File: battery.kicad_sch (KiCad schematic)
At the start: 27 parts, among them J2 Conn_01x02, U7 MP2637GR-P, U8 MAX17048G+T10

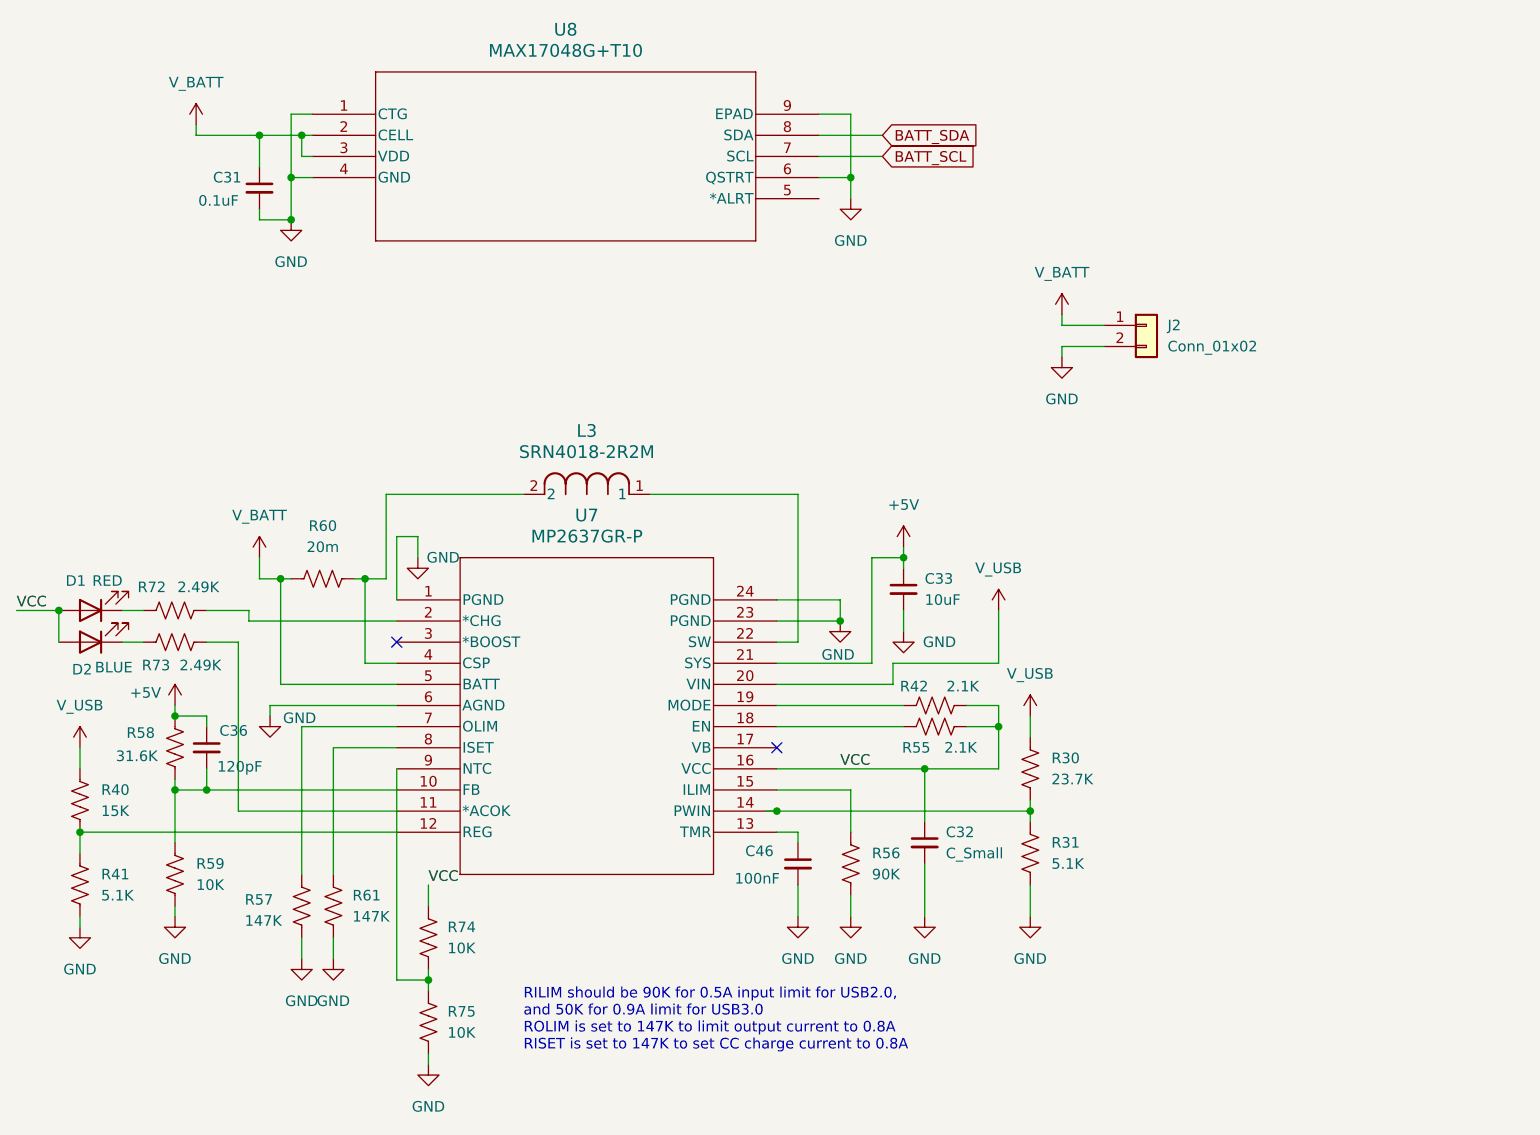
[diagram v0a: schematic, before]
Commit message: All footprints configured correctly. Next step is layout
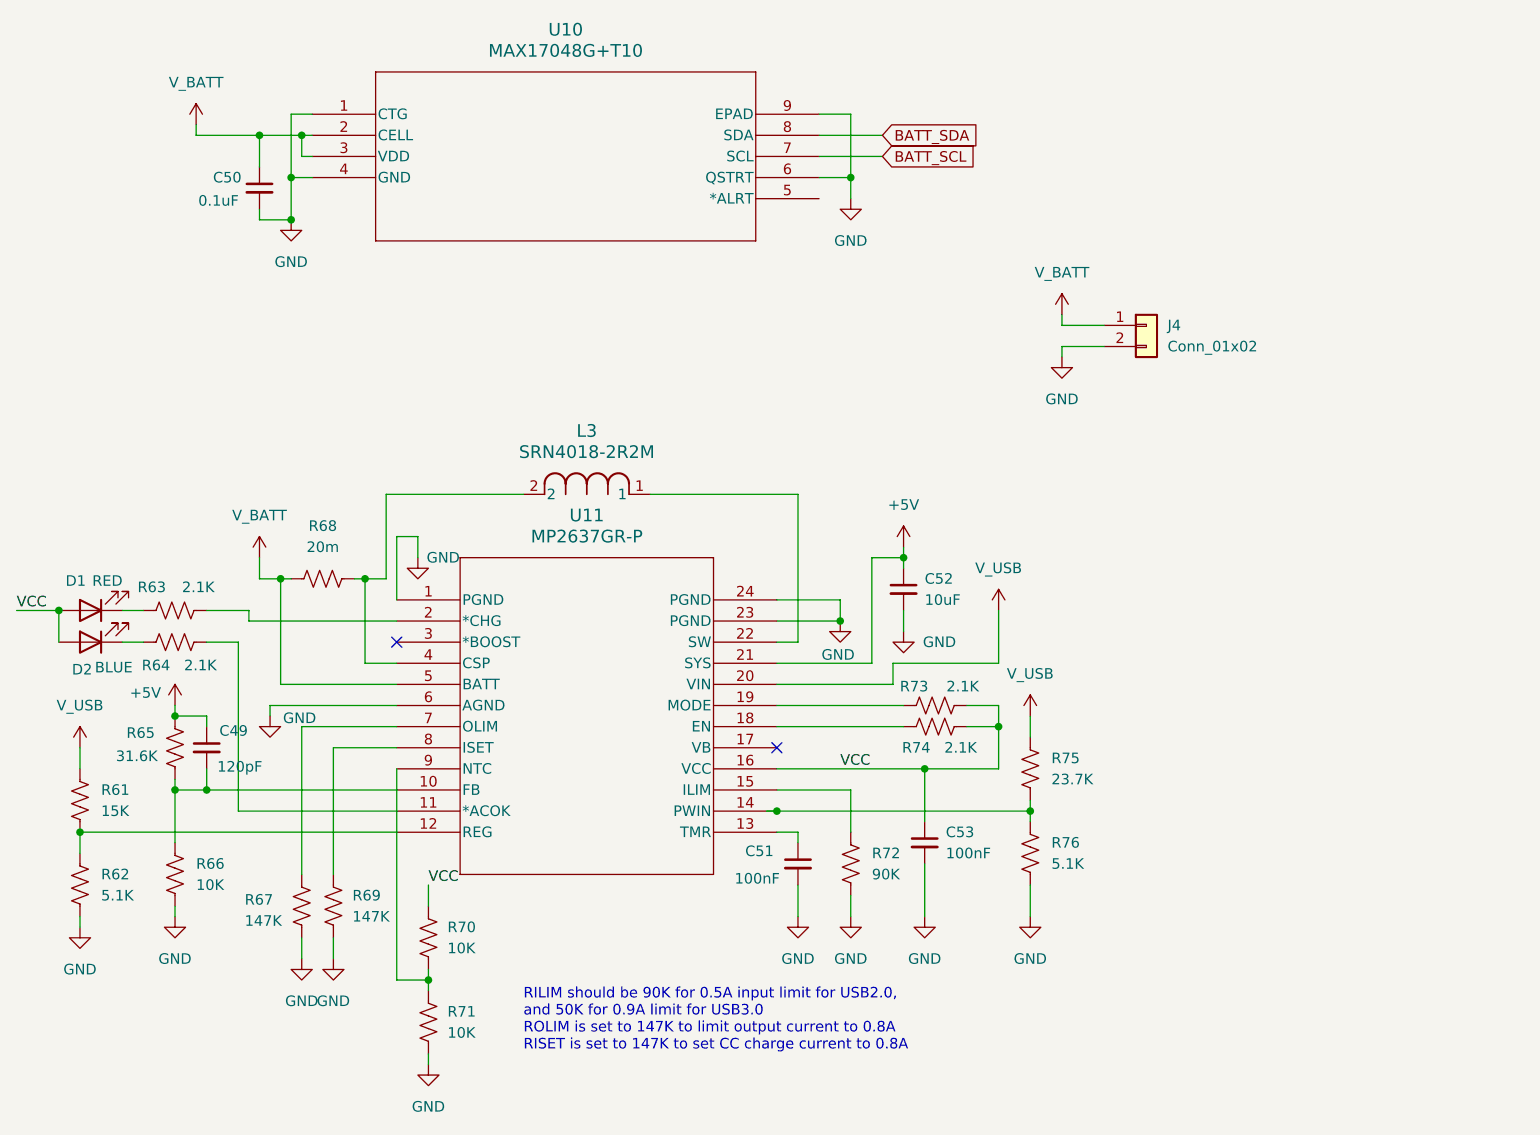
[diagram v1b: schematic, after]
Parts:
- C49: renamed from C36; footprint (none) -> Capacitor_SMD:C_0201_0603Metric_Pad0.64x0.40mm_HandSolder
- C50: renamed from C31; footprint (none) -> Capacitor_SMD:C_0201_0603Metric_Pad0.64x0.40mm_HandSolder
- C51: renamed from C46; footprint (none) -> Capacitor_SMD:C_0201_0603Metric_Pad0.64x0.40mm_HandSolder
- C52: renamed from C33; footprint (none) -> Capacitor_SMD:C_0201_0603Metric_Pad0.64x0.40mm_HandSolder
- C53: renamed from C32; value C_Small -> 100nF; footprint (none) -> Capacitor_SMD:C_0201_0603Metric_Pad0.64x0.40mm_HandSolder
- D1, D2: footprint (none) -> LED_SMD:LED_0805_2012Metric
- R61: renamed from R40; footprint (none) -> Resistor_SMD:R_0201_0603Metric_Pad0.64x0.40mm_HandSolder
- R62: renamed from R41; footprint (none) -> Resistor_SMD:R_0201_0603Metric_Pad0.64x0.40mm_HandSolder
- R63: renamed from R72; value 2.49K -> 2.1K; footprint (none) -> Resistor_SMD:R_0201_0603Metric_Pad0.64x0.40mm_HandSolder
- R64: renamed from R73; value 2.49K -> 2.1K; footprint (none) -> Resistor_SMD:R_0201_0603Metric_Pad0.64x0.40mm_HandSolder
- R65: renamed from R58; footprint (none) -> Resistor_SMD:R_0201_0603Metric_Pad0.64x0.40mm_HandSolder
- R66: renamed from R59; footprint (none) -> Resistor_SMD:R_0201_0603Metric_Pad0.64x0.40mm_HandSolder
- R67: renamed from R57; footprint (none) -> Resistor_SMD:R_0201_0603Metric_Pad0.64x0.40mm_HandSolder
- R68: renamed from R60; footprint (none) -> Resistor_SMD:R_0508_1220Metric_Pad1.12x2.15mm_HandSolder
- R69: renamed from R61; footprint (none) -> Resistor_SMD:R_0201_0603Metric_Pad0.64x0.40mm_HandSolder
- R70: renamed from R74; footprint (none) -> Resistor_SMD:R_0201_0603Metric_Pad0.64x0.40mm_HandSolder
- R71: renamed from R75; footprint (none) -> Resistor_SMD:R_0201_0603Metric_Pad0.64x0.40mm_HandSolder
- R72: renamed from R56; footprint (none) -> Resistor_SMD:R_0201_0603Metric_Pad0.64x0.40mm_HandSolder
- R73: renamed from R42; footprint (none) -> Resistor_SMD:R_0201_0603Metric_Pad0.64x0.40mm_HandSolder
- R74: renamed from R55; footprint (none) -> Resistor_SMD:R_0201_0603Metric_Pad0.64x0.40mm_HandSolder
- R75: renamed from R30; footprint (none) -> Resistor_SMD:R_0201_0603Metric_Pad0.64x0.40mm_HandSolder
- R76: renamed from R31; footprint (none) -> Resistor_SMD:R_0201_0603Metric_Pad0.64x0.40mm_HandSolder
- renumbered J2 to J4, U8 to U10, U7 to U11

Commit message: In the middle of layout. WIP
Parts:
- added TP7: V_USB_TP, TestPoint:TestPoint_Pad_D1.5mm, symbol Connector:TestPoint
- added TP8: V_BATT_TP, TestPoint:TestPoint_Pad_D1.5mm, symbol Connector:TestPoint
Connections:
- net V_BATT: now also TP8.1
- net V_USB: now also TP7.1
- no-connect marks 2 -> 3

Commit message: Breakthrough in PCB layout. WIP
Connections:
- net SW: now reaches L3.1, U11.22 (SW)
- net L3: now reaches L3.2, R68.2, U11.4 (CSP)
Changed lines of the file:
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@@
+		)
+	)
+	(label "+5V"
+		(at 118.11 99.06 0)
+		(fields_autoplaced yes)
+		(effects
+			(font
+				(size 1.27 1.27)
+			)
+			(justify left bottom)
+		)
+		(property "Netclass" "Power"
+			(at 118.11 100.33 0)
+			(effects
+				(font
+					(size 1.27 1.27)
+					(italic yes)
+				)
+				(justify left)
+			)
+		)
+	)
+	(label "V_BATT"
+		(at 46.99 96.52 0)
+		(fields_autoplaced yes)
+		(effects
+			(font
+				(size 1.27 1.27)
+			)
+			(justify left bottom)
+		)
+		(property "Netclass" "Power"
+			(at 46.99 97.79 0)
+			(effects
+				(font
+					(size 1.27 1.27)
+					(italic yes)
+				)
+				(justify left)
+			)
 		)
 	)
@@
 		)
 	)
+	(label "L3"
+		(at 66.04 82.55 0)
+		(fields_autoplaced yes)
+		(effects
+			(font
+				(size 1.27 1.27)
+			)
+			(justify left bottom)
+		)
+		(property "Netclass" "Power"
+			(at 66.04 83.82 0)
+			(effects
+				(font
+					(size 1.27 1.27)
+					(italic yes)
+				)
+				(justify left)
+			)
+		)
+	)
+	(label "V_USB"
+		(at 133.35 100.33 0)
+		(fields_autoplaced yes)
+		(effects
+			(font
+				(size 1.27 1.27)
+			)
+			(justify left bottom)
+		)
+		(property "Netclass" "Power"
+			(at 133.35 101.6 0)
+			(effects
+				(font
+					(size 1.27 1.27)
+					(italic yes)
+				)
+				(justify left)
+			)
+		)
+	)
+	(label "SW"
+		(at 109.22 87.63 0)
+		(fields_autoplaced yes)
+		(effects
+			(font
+				(size 1.27 1.27)
+			)
+			(justify left bottom)
+		)
+		(property "Netclass" "Power"
+			(at 109.22 88.9 0)
+			(effects
+				(font
+					(size 1.27 1.27)
+					(italic yes)
+				)
+				(justify left)
+			)
+		)
+	)

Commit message: Board is fully routed
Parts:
- removed J4: Conn_01x02, Connector_JST:JST_PH_S2B-PH-SM4-TB_1x02-1MP_P2.00mm_Horizontal, symbol Connector_Generic:Conn_01x02
- added J4: S2B-PH-SM4-TB_LF__SN_, S2B-PH-SM4-TB_LF__SN_:JST_S2B-PH-SM4-TB_LF__SN_, symbol S2B-PH-SM4-TB:S2B-PH-SM4-TB_LF__SN_
- R68: value 20m -> 20m - WSL1206R0200FEA; footprint Resistor_SMD:R_0508_1220Metric_Pad1.12x2.15mm_HandSolder -> Resistor_SMD:R_1206_3216Metric
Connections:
- net GND: now also J4.2, J4.S1 (SHIELD), J4.S2 (SHIELD__1)
- net V_BATT: now also J4.1
